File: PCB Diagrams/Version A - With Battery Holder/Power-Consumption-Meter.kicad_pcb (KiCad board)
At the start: 2 copper layers, 99.1 x 113 mm, 36 parts, among them J1 Jack_DC, J10 01x02, J11 01x02, J12 01x02, J13 01x02, J2 01x02, J3 01x02, J4 USB_A, J5 Jack_DC, J6 Jack_DC, J7 USB_B_Mini, J8 USB_B_Micro, J9 01x04, SW1 SW_SPDT, SW2 SW_Push, U1 INA219_Module, U2 Display_5641BS

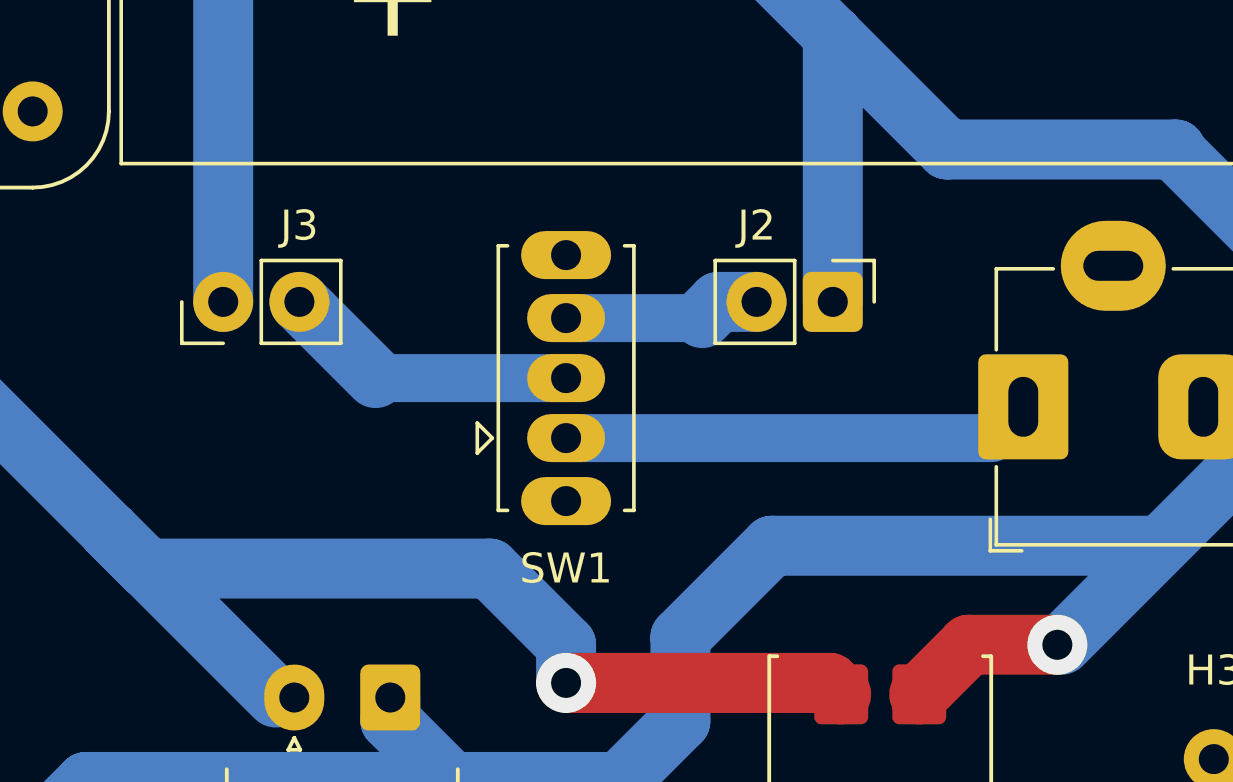
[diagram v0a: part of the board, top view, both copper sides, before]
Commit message: update PCB connectors
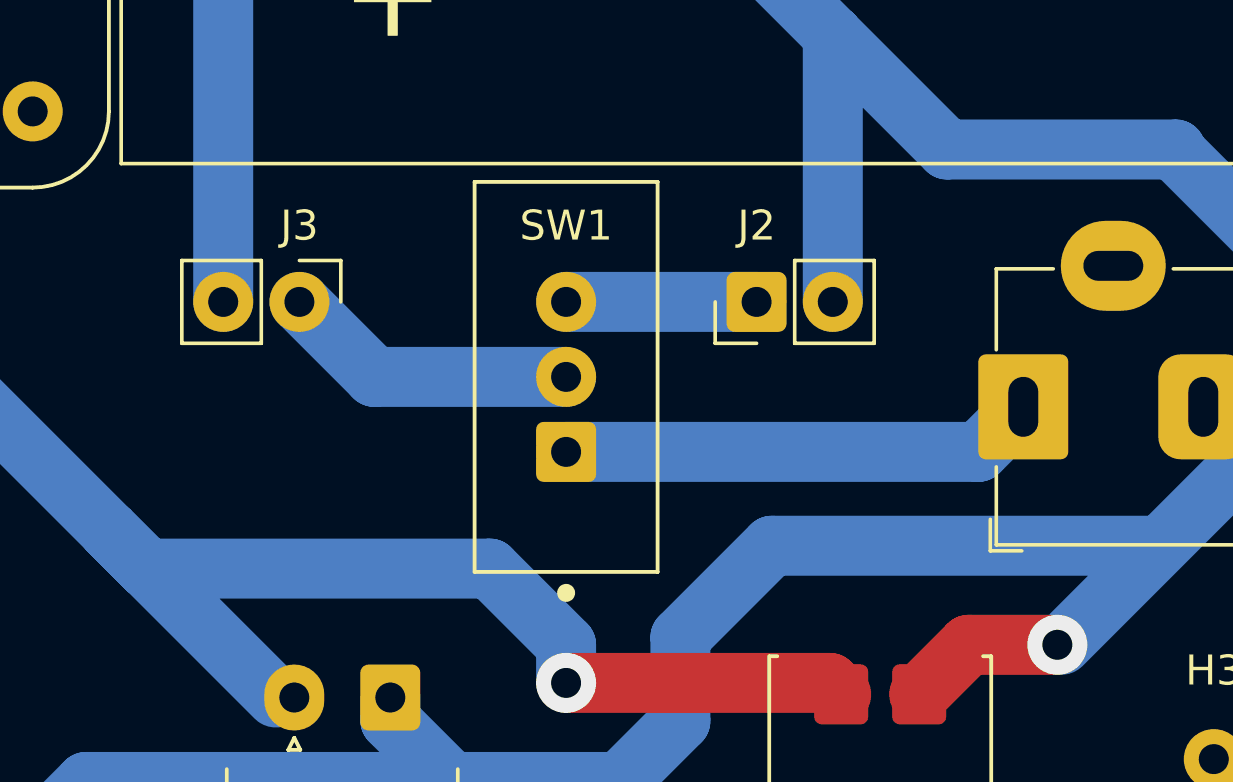
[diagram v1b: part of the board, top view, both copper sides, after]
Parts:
- J2: value 01x02 -> BAT_IN
- J3: value 01x02 -> PWR_BTN
- SW1: value SW_SPDT -> SW_Slide; footprint Button_Switch_THT:SW_Slide_SPDT_Straight_CK_OS102011MS2Q -> Custom:Switch_Slide_SPDT_Straight_TE_1825159_1
- moved J2 2.54 mm to (176.5, 125.7), turned to 90 degrees
- moved J3 2.54 mm to (161.3, 125.7), turned to -90 degrees
- moved SW1 2.04 mm to (170.2, 128.2)
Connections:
- J2 pad 1: GND -> Net-(BAT1-+)
- J2 pad 2: Net-(BAT1-+) -> GND
- J3 pad 1: PWR -> Net-(J3-Pin_1)
- J3 pad 2: Net-(J3-Pin_2) -> PWR
- SW1 pad 2: Net-(J3-Pin_2) -> Net-(J3-Pin_1)
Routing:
- net Net-(J3-Pin_2): track 9.94 -> 0.00 mm
- net Net-(J3-Pin_1): track 0.00 -> 9.93 mm
- net Net-(J1-Pad1): track 15.7 -> 17.3 mm

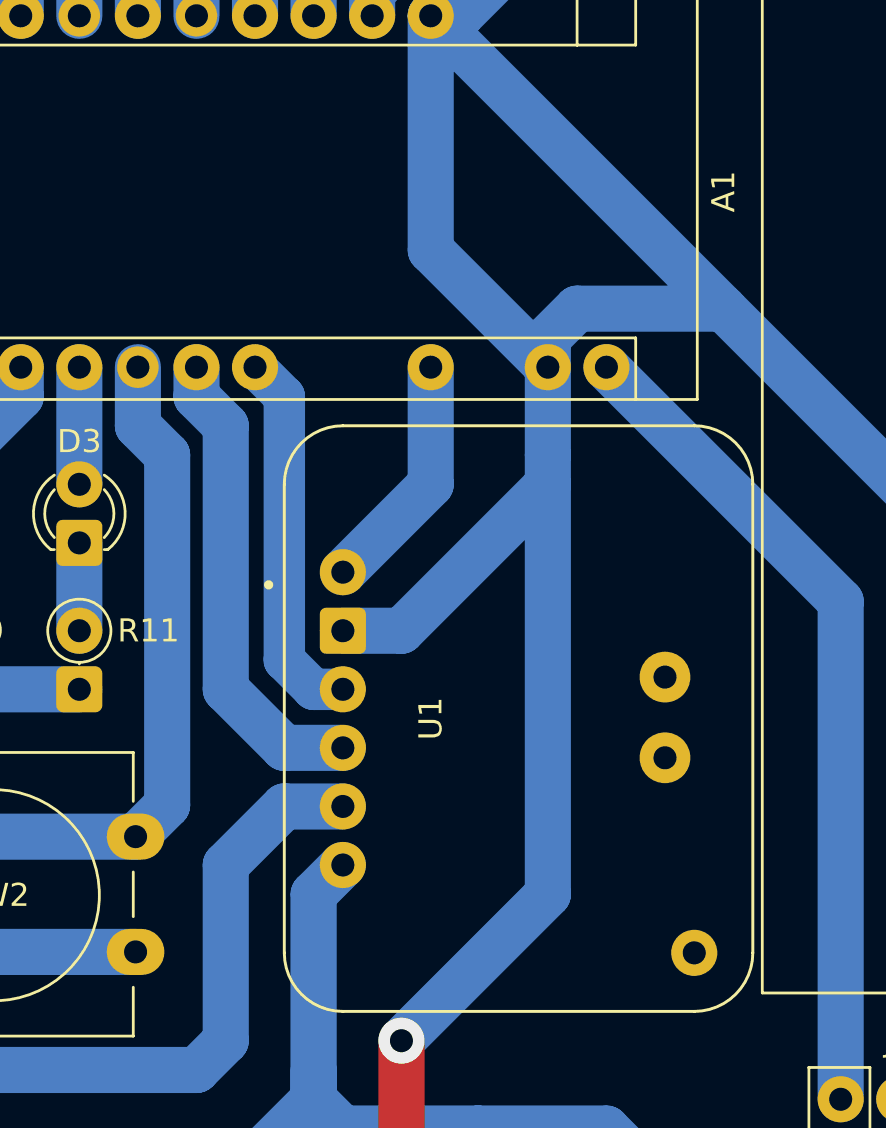
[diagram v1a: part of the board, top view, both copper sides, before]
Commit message: Adding PCB building and assembly pictures
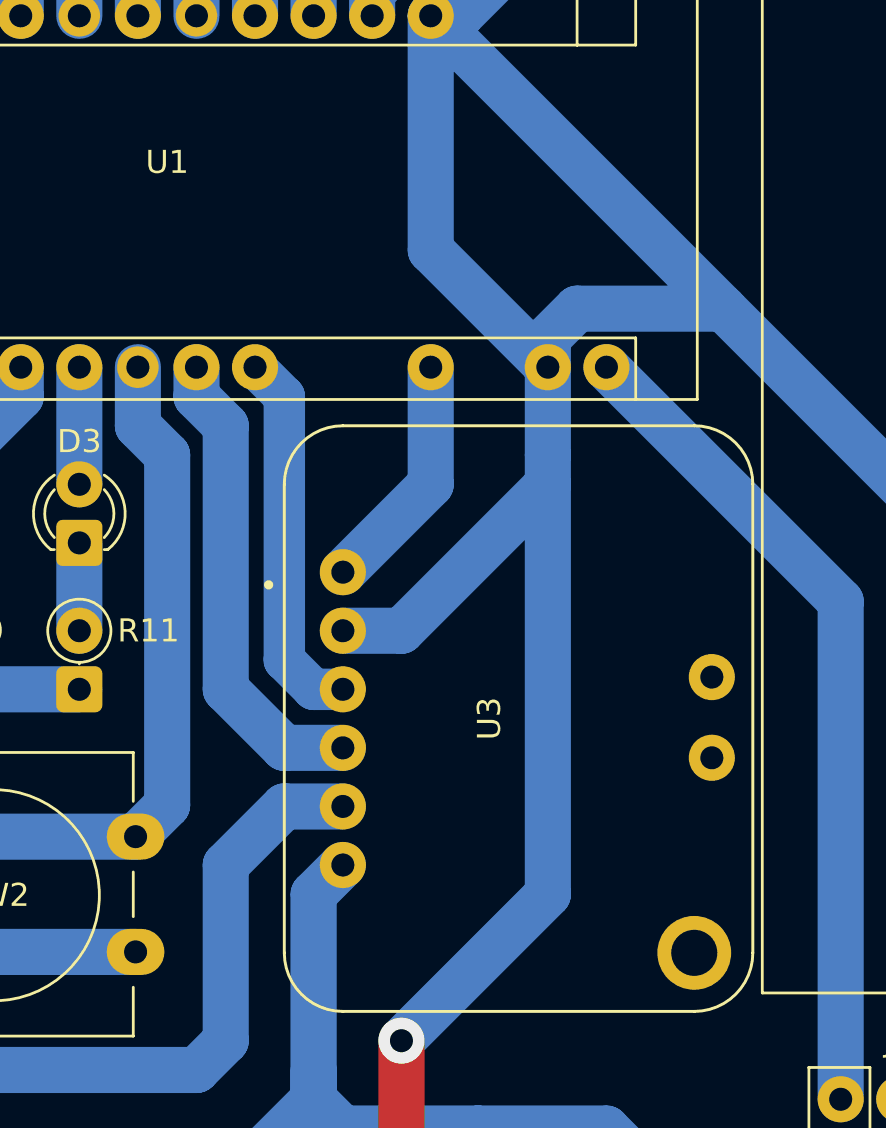
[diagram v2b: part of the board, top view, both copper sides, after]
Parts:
- removed the U1 at (144.8, 109.2)
- added U3: INA219_Module, Custom:INA219_Module_Generic, F.Cu at (144.8, 109.2)
- renumbered A1 to U1
